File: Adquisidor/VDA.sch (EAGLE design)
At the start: 109 parts, among them J1 USB-2.0, J3 FTSH-107-01-L-DV-K-A, SW1 DSHP03TSGER, U1 SN74LVC1G175, U2 CP2102N-28, U3 STM32F373CBT6, U4 LP5907MFX-3.3/NOPB, U5 ISO7721DR, U6 LP5907MFX-3.3/NOPB, U7 TL072, U8 LM13700, U9 REF3433IDBVR

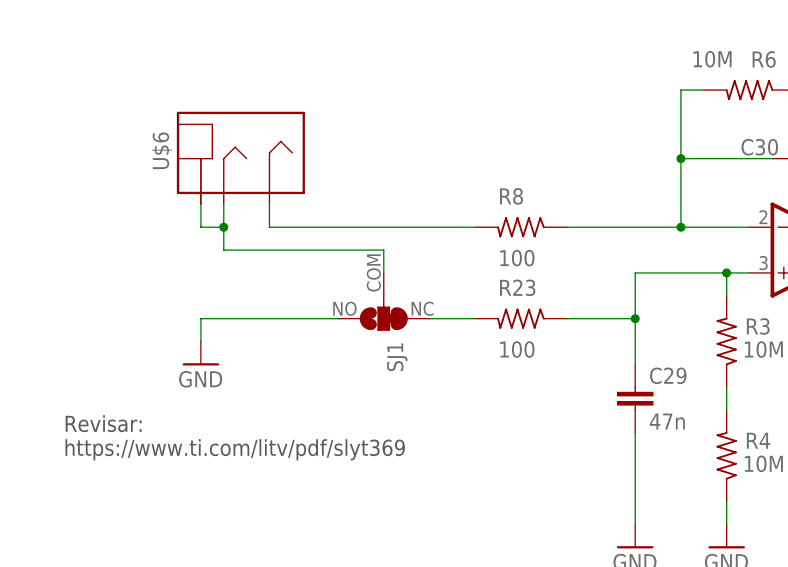
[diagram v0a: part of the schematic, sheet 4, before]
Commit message: panel frontal y posterior listos
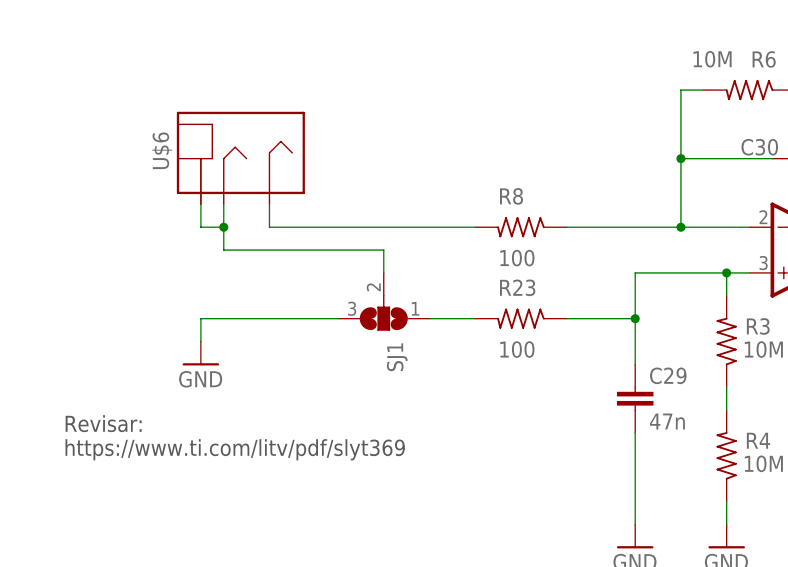
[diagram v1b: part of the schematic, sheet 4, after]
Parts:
- SJ1: device property-pads:SJ-PS -> jumper:SJ2W
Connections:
- net GND: now also SJ1.3; no longer SJ1.NO
- net N$17: now also SJ1.1; no longer SJ1.NC
- net N$6: now also SJ1.2; no longer SJ1.COM
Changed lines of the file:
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@@
 <part name="+3V42" library="property-supply" library_urn="urn:adsk.eagle:library:35374593" deviceset="+3V3" device=""/>
 <part name="GND54" library="supply1" library_urn="urn:adsk.eagle:library:371" deviceset="GND" device=""/>
-<part name="SJ4" library="jumper" library_urn="urn:adsk.eagle:library:252" deviceset="SJ" device="" package3d_urn="urn:adsk.eagle:package:15471/1"/>
+<part name="SJ4" library="jumper" library_urn="urn:adsk.eagle:library:46141633" deviceset="SJ" device="" package3d_urn="urn:adsk.eagle:package:46141762/3"/>
 <part name="C14" library="Property-standar" library_urn="urn:adsk.eagle:library:20126172" deviceset="C" device="_0603" package3d_urn="urn:adsk.eagle:package:20146986/3" value="100n"/>
 <part name="R20" library="Property-standar" library_urn="urn:adsk.eagle:library:20126172" deviceset="R" device="_0603" package3d_urn="urn:adsk.eagle:package:39983384/2" value="100"/>
@@
 <part name="C81" library="Property-standar" library_urn="urn:adsk.eagle:library:20126172" deviceset="C-TANTALUM" device="_A_3216" package3d_urn="urn:adsk.eagle:package:22275356/3" value="47u"/>
 <part name="GND7" library="supply1" library_urn="urn:adsk.eagle:library:371" deviceset="GND" device=""/>
-<part name="SJ16" library="jumper" library_urn="urn:adsk.eagle:library:252" deviceset="SJ" device="" package3d_urn="urn:adsk.eagle:package:15471/1"/>
+<part name="SJ16" library="jumper" library_urn="urn:adsk.eagle:library:46141633" deviceset="SJ" device="" package3d_urn="urn:adsk.eagle:package:46141762/3"/>
 <part name="U4" library="property-power" library_urn="urn:adsk.eagle:library:35647964" deviceset="LDO1" device="SOT23-5_1" package3d_urn="urn:adsk.eagle:package:35647967/5" value="LP5907MFX-3.3/NOPB"/>
 <part name="GND29" library="supply1" library_urn="urn:adsk.eagle:library:371" deviceset="GND" device=""/>
@@
 <attribute name="TYPE" value="Schotky"/>
 </part>
-<part name="SJ6" library="jumper" library_urn="urn:adsk.eagle:library:252" deviceset="SJ" device="" package3d_urn="urn:adsk.eagle:package:15471/1"/>
+<part name="SJ6" library="jumper" library_urn="urn:adsk.eagle:library:46141633" deviceset="SJ" device="" package3d_urn="urn:adsk.eagle:package:46141762/3"/>
 <part name="U$1" library="Frames" library_urn="urn:adsk.eagle:library:46102009" deviceset="FRAMES" device=""/>
 <part name="U$2" library="Frames" library_urn="urn:adsk.eagle:library:46102009" deviceset="FRAMES" device=""/>
@@
 <part name="C32" library="Property-standar" library_urn="urn:adsk.eagle:library:20126172" deviceset="C" device="_0603" package3d_urn="urn:adsk.eagle:package:20146986/3" value="470n"/>
 <part name="GND33" library="supply1" library_urn="urn:adsk.eagle:library:371" deviceset="GND" device=""/>
-<part name="SJ1" library="property-pads" library_urn="urn:adsk.eagle:library:35645945" deviceset="SJ-PS" device="" package3d_urn="urn:adsk.eagle:package:39849077/2"/>
+<part name="SJ1" library="jumper" library_urn="urn:adsk.eagle:library:46141633" deviceset="SJ2W" device="" package3d_urn="urn:adsk.eagle:package:46141746/2"/>
 <part name="U8" library="property_analog" library_urn="urn:adsk.eagle:library:46112994" deviceset="LM13700" device="" package3d_urn="urn:adsk.eagle:package:46113006/2"/>
 <part name="R12" library="Property-standar" library_urn="urn:adsk.eagle:library:20126172" deviceset="R" device="_0603" package3d_urn="urn:adsk.eagle:package:39983384/2" value="30k"/>
@@
 <attribute name="V" value="16V"/>
 </part>
-<part name="SJ2" library="jumper" library_urn="urn:adsk.eagle:library:252" deviceset="SJ" device="" package3d_urn="urn:adsk.eagle:package:15471/1"/>
+<part name="SJ2" library="jumper" library_urn="urn:adsk.eagle:library:46141633" deviceset="SJ" device="" package3d_urn="urn:adsk.eagle:package:46141762/3"/>
 <part name="U9" library="Power-Supply" library_urn="urn:adsk.eagle:library:46110086" deviceset="REF3433IDBVR" device="" package3d_urn="urn:adsk.eagle:package:46141433/2"/>
 <part name="GND44" library="supply1" library_urn="urn:adsk.eagle:library:371" deviceset="GND" device=""/>
-<part name="R29" library="Property-standar" library_urn="urn:adsk.eagle:library:20126172" deviceset="R-VARIABLE" device="09VR1B" package3d_urn="urn:adsk.eagle:package:46141532/2"/>
+<part name="R29" library="Property-standar" library_urn="urn:adsk.eagle:library:20126172" deviceset="R-VARIABLE" device="09VR1B" package3d_urn="urn:adsk.eagle:package:46141532/3"/>
 <part name="+3V3A2" library="property-supply" library_urn="urn:adsk.eagle:library:35374593" deviceset="+3V3A" device=""/>
 <part name="GND45" library="supply1" library_urn="urn:adsk.eagle:library:371" deviceset="GND" device=""/>
@@
 <pinref part="GND26" gate="1" pin="GND"/>
 <wire x1="30.48" y1="121.92" x2="30.48" y2="124.46" width="0.1524" layer="91"/>
-<pinref part="SJ1" gate="G$1" pin="NO"/>
+<pinref part="SJ1" gate="G$1" pin="3"/>
 <wire x1="45.72" y1="124.46" x2="30.48" y2="124.46" width="0.1524" layer="91"/>
 </segment>
@@
 <wire x1="30.48" y1="134.62" x2="30.48" y2="137.16" width="0.1524" layer="91"/>
 <wire x1="30.48" y1="134.62" x2="33.02" y2="134.62" width="0.1524" layer="91"/>
-<pinref part="SJ1" gate="G$1" pin="COM"/>
+<pinref part="SJ1" gate="G$1" pin="2"/>
 <wire x1="50.8" y1="129.54" x2="50.8" y2="132.08" width="0.1524" layer="91"/>
 <wire x1="50.8" y1="132.08" x2="33.02" y2="132.08" width="0.1524" layer="91"/>
@@
 <net name="N$17" class="0">
 <segment>
-<pinref part="SJ1" gate="G$1" pin="NC"/>
+<pinref part="SJ1" gate="G$1" pin="1"/>
 <wire x1="55.88" y1="124.46" x2="60.96" y2="124.46" width="0.1524" layer="91"/>
 <pinref part="R23" gate="G$1" pin="2"/>

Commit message: layout avanzado
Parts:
- removed C32: 470n, Property-standar:C_0603
- removed C39: 4u7, Property-standar:C_0603
- removed C40: 100n, Property-standar:C_0603
- removed C41: 10u, Property-standar:C_0603
- removed U9: REF3433IDBVR, Power-Supply:REF3433IDBVR
- added C42: 1u, Property-standar:C_0603
- added C43: 100n, Property-standar:C_0603
- added D1, D13, D14, D15, D16, D17, D6, D7, D8, D9: 1N4148, Property-standar:D-SOD123W
- added J2: CONVERT-2X6-2.54MM-FEMALE, property-connectors:CONVERT-2X6-2.54MM-FEMALE
- added J4: CONVERT-1X4-2.54MM-MALE_HOLES, property-connectors:CONVERT-1X4-2.54MM-MALE_HOLES
- added J5: F0504-H-05-10G-R, property-connectors:F0504-H-05-10G-R
- added Q1, Q2: BC856, Property-standar:PNP_SOT23
- added R30: 33k, Property-standar:R_0603
- added R31: 3k9, Property-standar:R_0603
- added R32: 100, Property-standar:R_0603
- added R33: 500, Property-standar:R-VARIABLE_VTRIM
- added R34: 1k, Property-standar:R_0603
- added R35, R37: TBD, Property-standar:R_0603
- added SJ3: (no value), jumper:SJ
- added TP10, TP5, TP6, TP7, TP8, TP9: TPTP16R, property-pads:TPTP16R
- C29, C30: value 47n -> 100n; DESCRIPTION (none) -> NP0
- C31: value 3.3u -> 47n
- R10: value 2k -> 150
- R11: value 2k -> 100
- R12: value 30k -> 100k
- R13: value 10k -> TBD
- R14: value 30k -> DNP
- R23, R4, R6, R8: DESCRIPTION (none) -> FILM
- R29: value (none) -> 10k; MPN (none) -> RK09K1110077
- R3: value 10M -> TBD; device Property-standar:R_0603 -> Property-standar:R-VARIABLE_VTRIM
- R7: value 10M -> TBD
- R9: value 2k -> 33k
- SJ1: device jumper:SJ2W -> property-pads:SJ-PSS
- SJ2: device jumper:SJ -> property-pads:SJ-PSS
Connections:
- net ON_MODE renamed SW_1
- net RS_MODE renamed SW_2
- net SP_MODE renamed SW_3
- removed net DAC_OUT: R14.1
- removed net GND1: C30.2, R7.1, R9.2, U71.OUT
- removed net LED_ACQ: D12.K
- removed net LED_PWR: D10.K
- removed net MANUAL_GAIN: R29.C
- removed net PV: U3.PD8
- removed net SP1: U3.PB1
- new net ACQ_LED: J5.4, R36.1, U3.PB6
- new net DAC1_CH1: R9.2, TP7.TP, U3.PA3
- new net DAC1_CH2: J2.9, U3.PA4
- new net DAC2_CH1: J2.5, U3.PA5
- new net I_ABC: Q1.C, U8_1.AMP_BIAS
- new net N$20: R33.2, R33.C, U8_1.-
- new net N$21: Q2.C, U8_1.D_BIAS
- new net N$22: R32.1, R33.1
- new net N$23: J5.2, SJ1.COM
- new net N$24: D6.A, Q2.B, R10.2
- new net N$27: R35.2, R37.1, U73.-IN
- new net OUT_CHARGE_AMP: C30.2, R30.1, R6.1, TP8.TP, U71.OUT
- new net OUT_OTA: C31.2, R12.1, U74.-IN, U8_1.OUT
- new net POWER_LED: J5.5, U3.PB7
- new net SDADC1_CH4: J2.3, U3.PB2
- new net SDADC1_CH5: D16.A, D17.K, R37.2, TP6.TP, U3.PB1, U73.OUT
- new net SDADC1_CH6: R29.C, TP10.TP, U3.PB0
- new net SDADC1_CH7: TP9.TP, U3.PE9
- new net SDADC1_CH8: J2.4, U3.PE8
- new net SDADC3_CH7: J2.7, U3.PB15
- new net SDADC3_CH8: J2.8, U3.PB14
- new net VREF_SDADC: C42.1, C43.1, SJ3.2, U3.VREFSD+
- net +3V3: now also J4.4, SJ1.NO; no longer R36.1, R5.1
- net +3V3A: now also D16.K, R13.2, R14.2, R29.2, SJ3.1; no longer R29.1, SJ2.1, U3.VREFSD+
- net +5V: now also D1.K, D13.K, D9.K, J2.1, J2.11, R34.2, R5.1, SJ1.NC; no longer C41.1, U9.EN, U9.IN
- net -5V: now also D7.A, D8.A, J2.12, J2.2, U8_2.D_BIAS; no longer R13.2
- net BOOT0: now also J5.3, R22.1, U1.Q
- net GND: now also C42.2, C43.2, D10.K, D12.K, D17.A, J2.10, J2.6, J4.2, J5.1, J5.SUP, R10.1, R11.2, R29.1, R31.2, R7.1, SJ2.NO, U$6.SLEEVE, U72.+IN; no longer C31.2, C39.2, C40.2, C41.2, R12.2, R29.2, SJ1.3, U9.GND_F, U9.GND_S
- net JCLK: now also J4.3
- net JTMS: now also J4.1
- net N$10: now also Q1.B, U72.OUT; no longer C32.1, R10.1, U74.OUT
- net N$11: now also Q2.E, R34.1; no longer C32.2, R11.1, U74.-IN
- net N$12: now also D1.A, D6.K; no longer R13.1, U8_1.E
- net N$13: now also R13.1, R3.1; no longer R14.2, U8_1.AMP_BIAS
- net N$16: now also D13.A, D14.K, D15.A, D8.K
- net N$17: now also D14.A, D15.K, D7.K, D9.A, SJ2.NC; no longer SJ1.1
- net N$18: now also R3.C, U73.+IN; no longer R22.1, U1.Q
- net N$19: now also R30.2, R31.1, U8_1.+; no longer C39.1, C40.1, SJ2.2, U9.OUT_F, U9.OUT_S
- net N$2: now also C31.1, R12.2, R35.1, TP5.TP, U74.OUT; no longer C29.1, R23.1, R3.2, U71.+IN
- net N$3: now also C29.1, R23.1, U71.+IN; no longer R3.1
- net N$5: now also R3.2; no longer R6.1
- net N$6: now also SJ2.COM; no longer SJ1.2, U$6.SLEEVE
- net N$7: now also Q1.E, R14.1, U72.-IN; no longer C31.1, R10.2, R11.2
- net N$9: now also R11.1, R32.2; no longer R12.1, U8_1.B, U8_1.OUT
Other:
- note added: "(0-3V3 -> 0-100uA)"
- note added: "4 Wire JTAG Debug"
- note added: "Amplifier and Offset"
- note added: "Current to Voltage"
- note added: "Expansion Connector"
- note added: "Front Panel Connector"
- note added: "Ganancia 0.16 - 2.5"
- note added: "ISOLATED UART"
- note added: "LPF fc=33Hz"
- note added: "Serial Wire Debug"
- note added: "Set Minimum current"
- note added: "Unused LM13700 1/2"
- note added: "Voltage - Current Converter"
- note added: "Voltage Controlled Amplifier"
- note added: "https://www.ti.com/litv/pdf/slyt369"
- note removed: "Revisar: https://www.ti.com/litv/pdf/slyt369"
- note removed: "SDADC1_AIN5P"
- note removed: "SDADC3_AIN6P"
- note removed: "Voltage Reference"
- moved on the sheet: C1, C19, C2, C20, C26, C27, C28, C29, C3, C30, C31, C33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

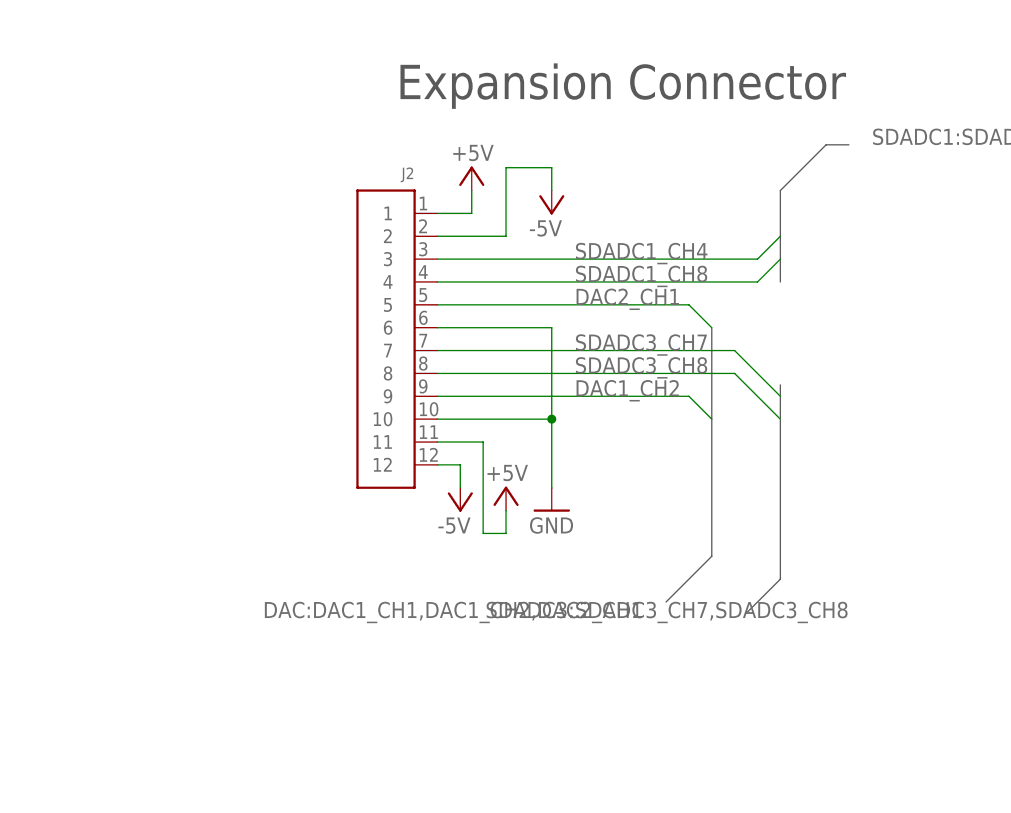
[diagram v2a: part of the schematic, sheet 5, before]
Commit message: cambio de conector para expansion
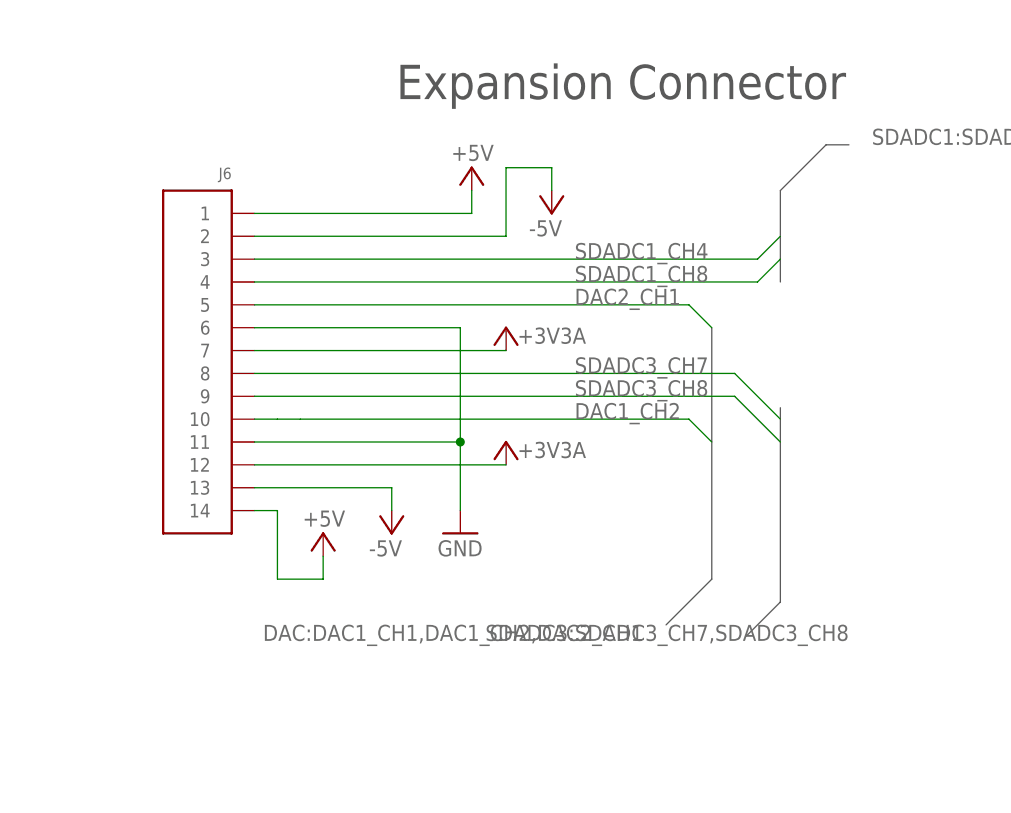
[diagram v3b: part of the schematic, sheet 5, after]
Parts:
- removed J2: CONVERT-2X6-2.54MM-FEMALE, property-connectors:CONVERT-2X6-2.54MM-FEMALE
- added J6: CONVERT-2X7-2.54MM-FEMALE, property-connectors:CONVERT-2X7-2.54MM-FEMALE
- R35: value TBD -> 1k
- R37: value TBD -> 2k2
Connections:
- net +3V3A: now also J6.12, J6.7
- net +5V: now also J6.1, J6.14; no longer J2.1, J2.11
- net -5V: now also J6.13, J6.2, U8_2.AMP_BIAS; no longer J2.12, J2.2, U8_2.D_BIAS
- net DAC1_CH2: now also J6.10; no longer J2.9
- net DAC2_CH1: now also J6.5; no longer J2.5
- net GND: now also J6.11, J6.6; no longer J2.10, J2.6
- net SDADC1_CH4: now also J6.3; no longer J2.3
- net SDADC1_CH8: now also J6.4; no longer J2.4
- net SDADC3_CH7: now also J6.8; no longer J2.7
- net SDADC3_CH8: now also J6.9; no longer J2.8

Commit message: layout terminado
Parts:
- R3: device Property-standar:R-VARIABLE_VTRIM -> Property-standar:R-VARIABLE-3.2X4; MPN (none) -> 3224W-1-103E
- R33: device Property-standar:R-VARIABLE_VTRIM -> Property-standar:R-VARIABLE-3.2X4; MPN (none) -> 3224W-1-501E
- renumbered U$6 to J2
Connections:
- net +3V3A: now also J6.14; no longer J6.12
- net +5V: now also J6.9; no longer J6.14
- net -5V: now also J6.8; no longer J6.13
- net DAC1_CH2: now also J6.12; no longer J6.10
- net GND: now also J6.13; no longer J6.11
- net SDADC3_CH7: now also J6.10; no longer J6.8
- net SDADC3_CH8: now also J6.11; no longer J6.9
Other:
- moved on the sheet: J6
